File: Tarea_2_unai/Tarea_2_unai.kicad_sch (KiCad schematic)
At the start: 0 parts

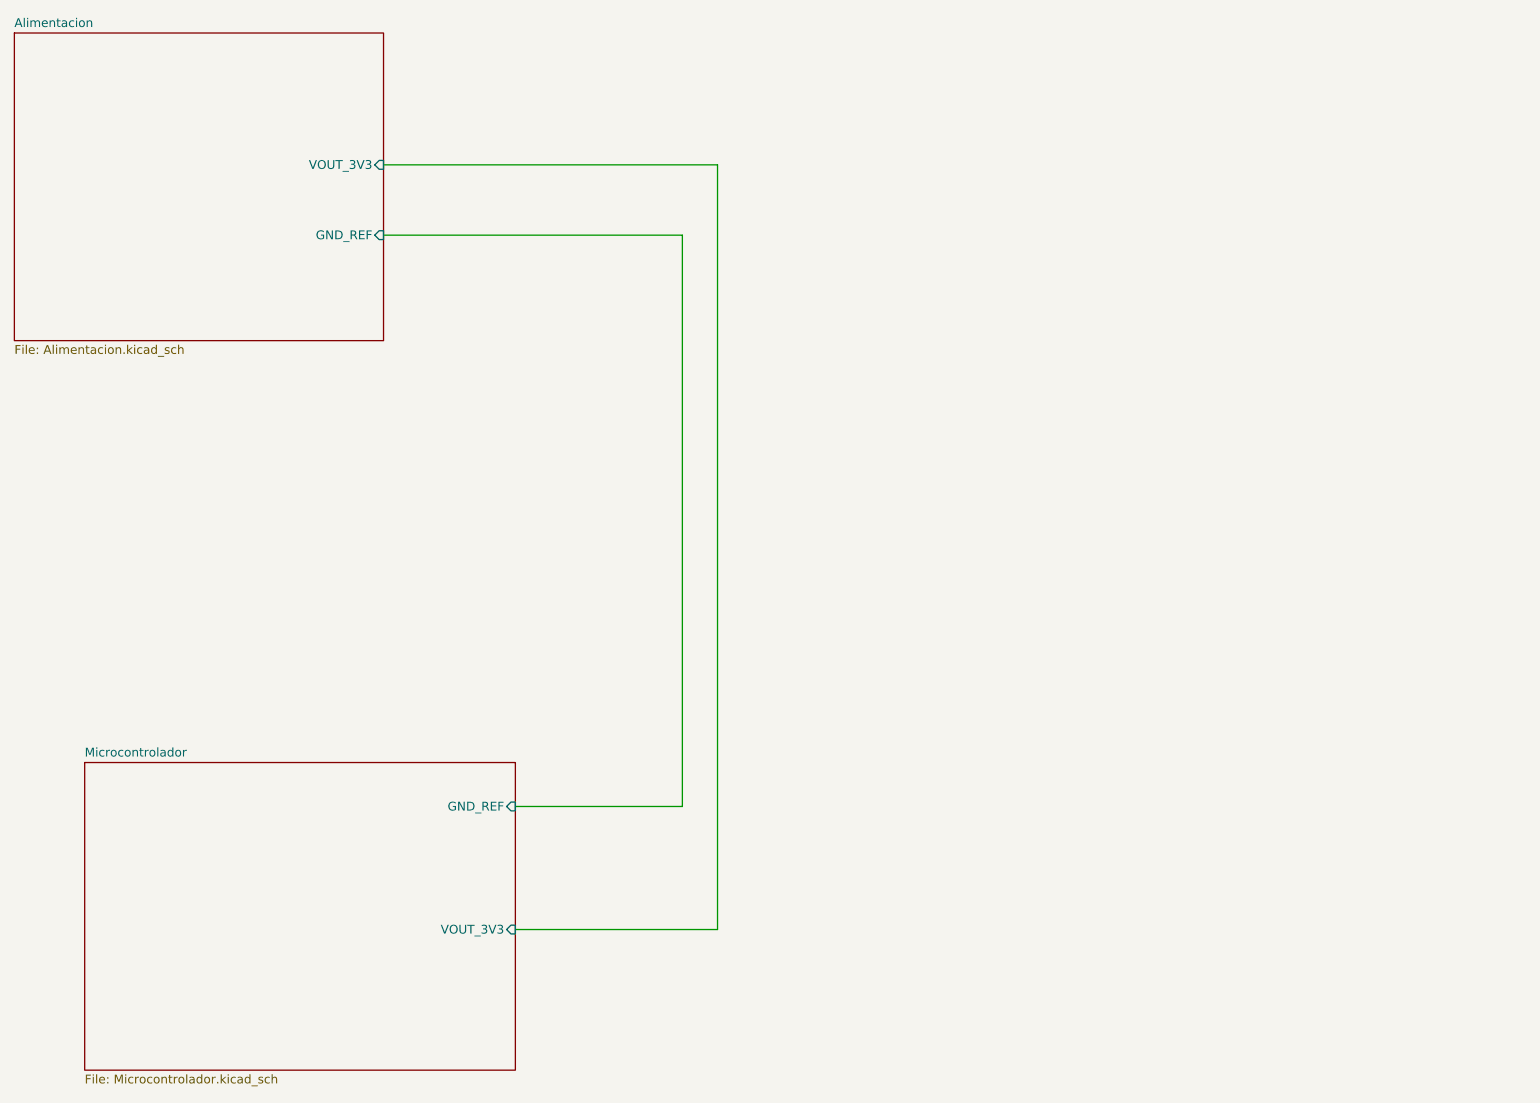
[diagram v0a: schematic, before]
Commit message: Sensores añadidos y nuevas capas añadidas
Falta por solucionar el enrutamiento de algunos pines de los sensores
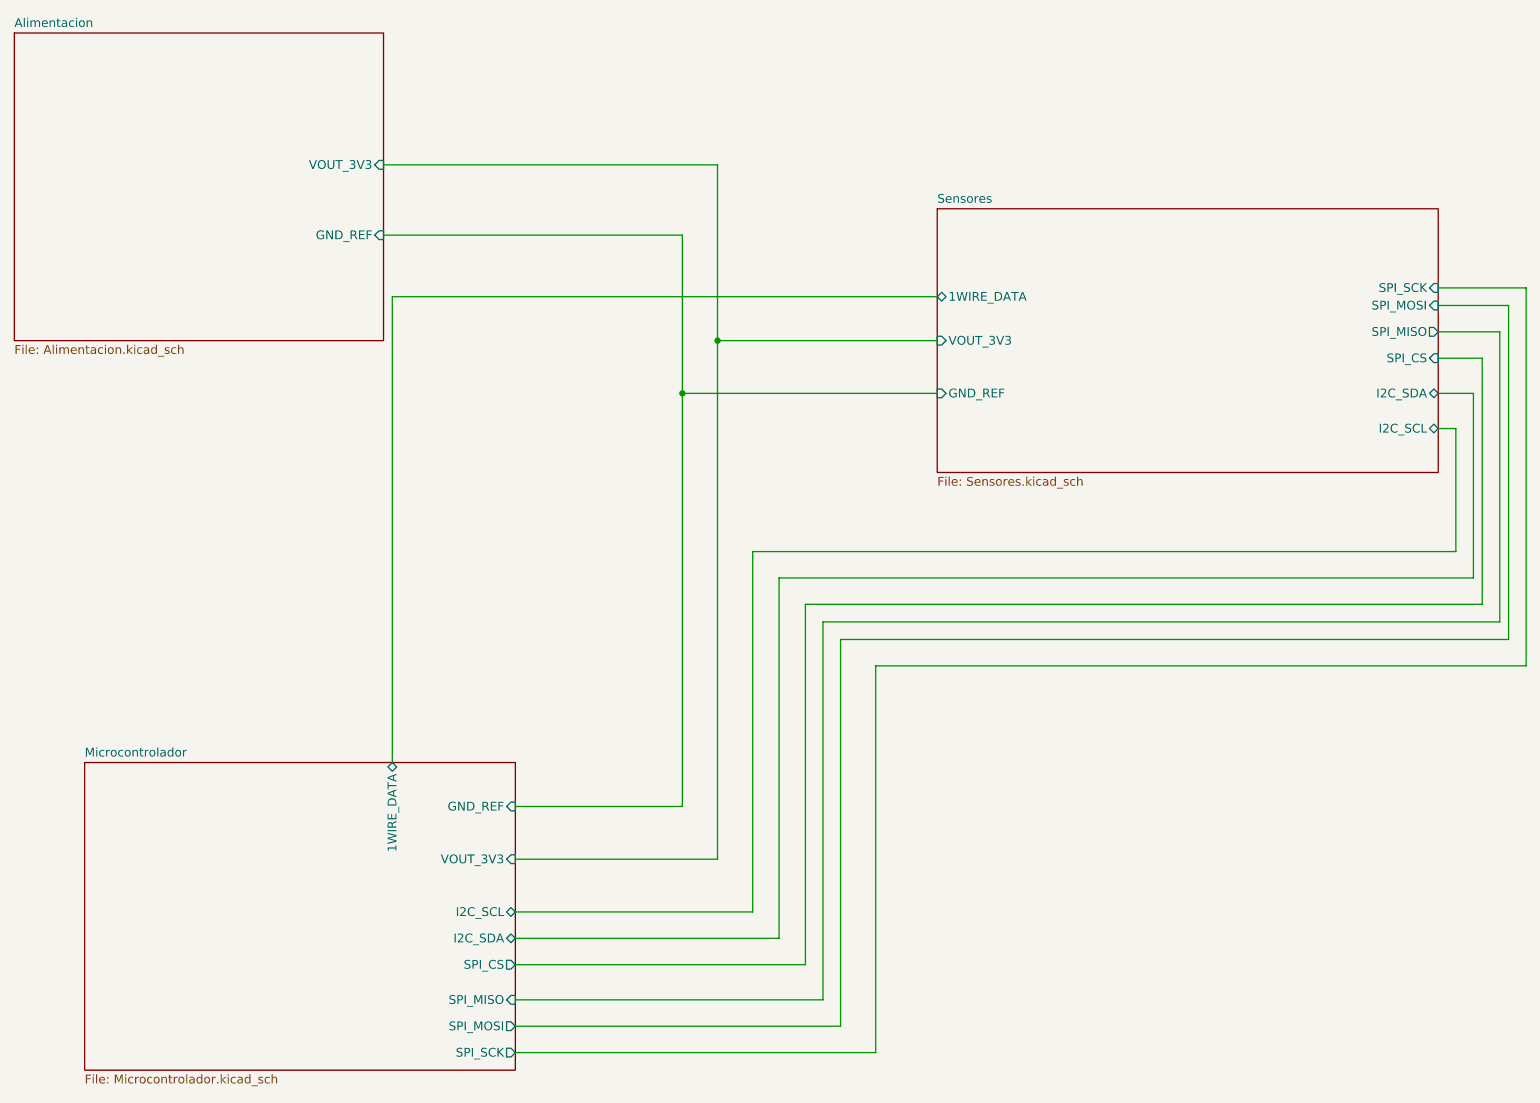
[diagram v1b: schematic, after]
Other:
- added sheet Sensores (Sensores.kicad_sch)
- sheet Microcontrolador ports: added 1WIRE_DATA, I2C_SCL, I2C_SDA, SPI_CS, SPI_MISO, SPI_MOSI, SPI_SCK; removed none
